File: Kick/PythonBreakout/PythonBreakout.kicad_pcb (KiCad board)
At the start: 4 copper layers, 29 x 37.8 mm, 15 parts, among them J1 SFML-115-02, J2 Conn_02x10_Odd_Even, U0 NOIP1SN1300A-QTI

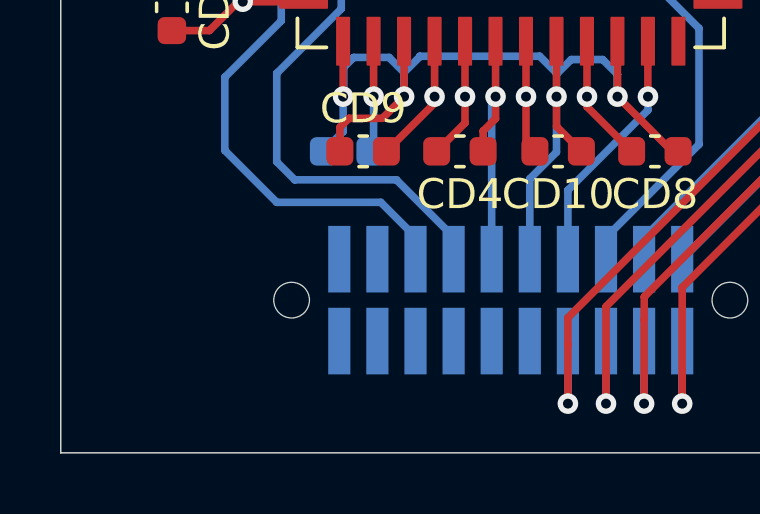
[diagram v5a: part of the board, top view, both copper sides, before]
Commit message: verificated and generated output products for both boards
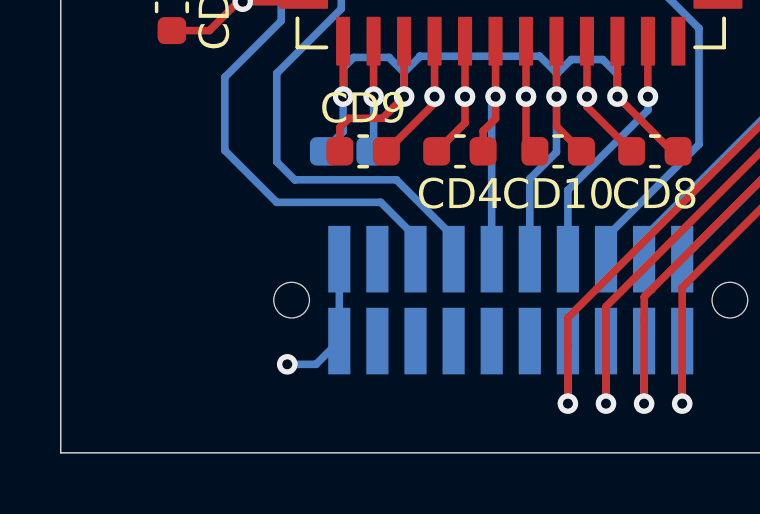
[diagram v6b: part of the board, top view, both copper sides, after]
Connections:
- J2 pad 1: unconnected-(J2-Pin_1-Pad1) -> GND
- J2 pad 2: unconnected-(J2-Pin_2-Pad2) -> GND
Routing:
- net GND: track 68.6 -> 73.4 mm, vias 13 -> 14
